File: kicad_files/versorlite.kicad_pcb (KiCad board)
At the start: 4 copper layers, 33 x 81.3 mm, 138 parts, among them J1 Conn_01x01_Socket, J10 IGN_2, J3 RFD900ux 10 Pin Header, J4 Conn_ARM_JTAG_SWD_10, J5 RFD900ux 3 Pin Power Select, J6 USB_C_Receptacle_USB2.0_16P, J7 Micro_SD_Card_Det2, J8 Conn_01x02_Socket, J9 IGN_1, Q1 FDMC510P-MS, Q2 AO3400A, Q3 AO3400A, SW1 SW_Push, SW2 SW_Push, U1 STM32F407VGTx, U10 W25Q128JVS, U11 LT1963AxST-3.3, U12 AP63205WU, U13 74LVC1G125, U2 MS5611-01BA, U3 BMI088, U4 MMC5983MA, U5 MAX-M10S, U6 BMP388, U7 LSM6DSM, U9 WE-TVS-82400102, Y1 LFXTAL036869Reel 8MHz Crystal

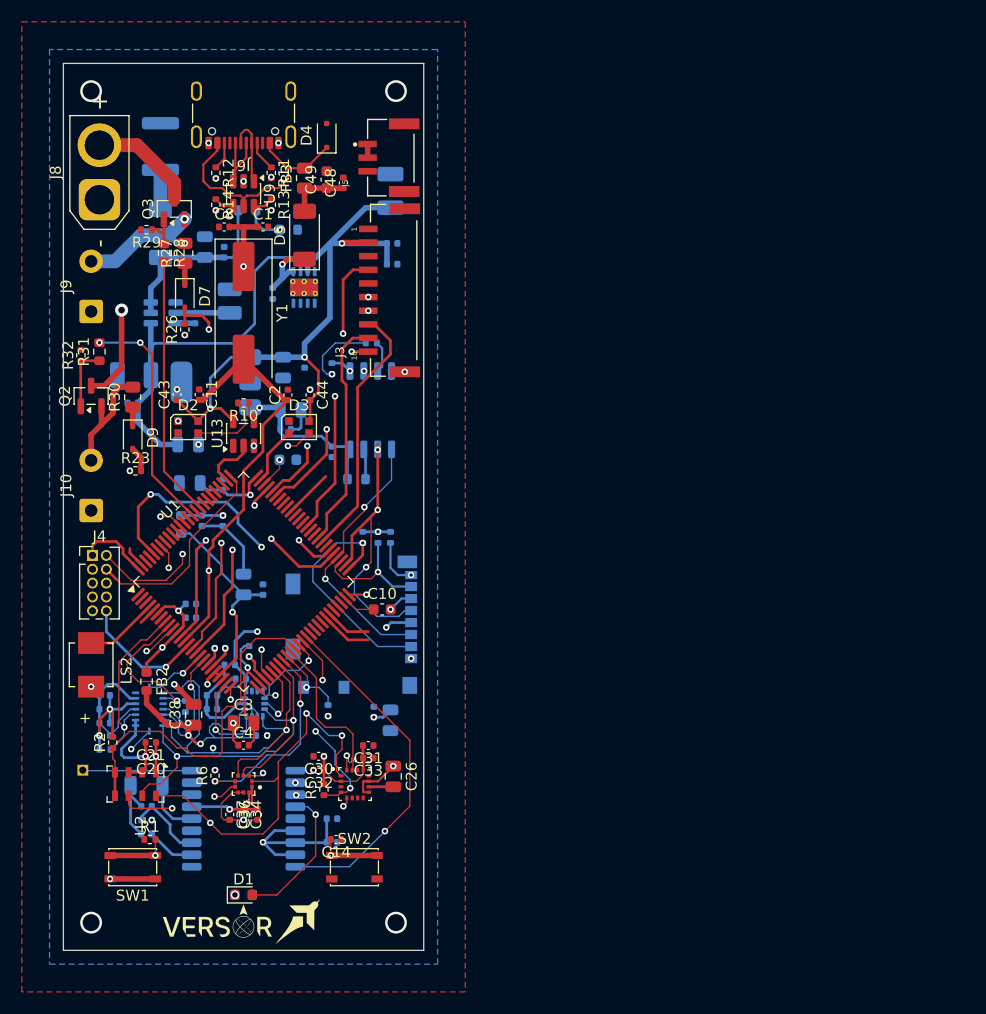
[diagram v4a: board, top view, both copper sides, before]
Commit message: fix mosfet, power traces, remove capacitors
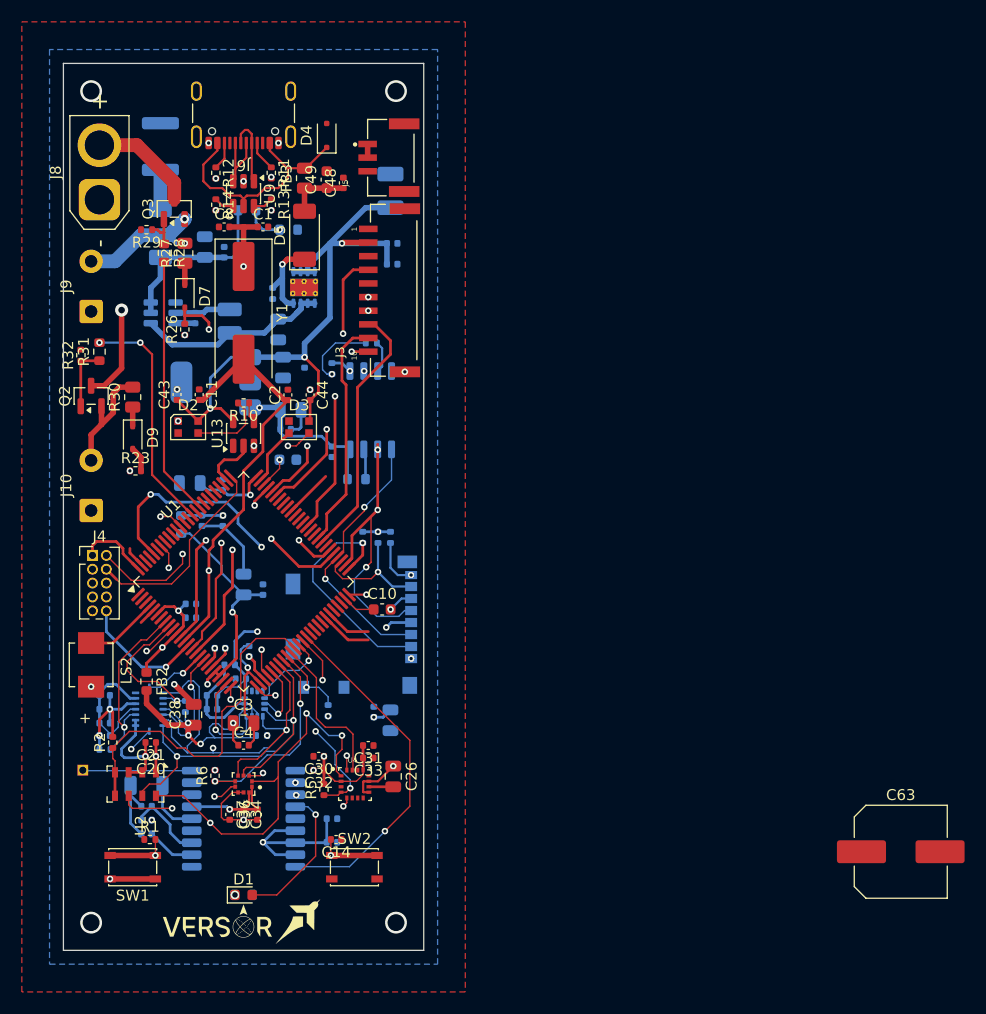
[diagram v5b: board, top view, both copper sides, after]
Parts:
- removed C57: 100μf, Capacitor_Tantalum_SMD:CP_EIA-3528-21_Kemet-B
- removed C59: 100nf, Capacitor_SMD:C_0402_1005Metric
- added C63: 470uF, Capacitor_SMD:C_Elec_8x10.2, F.Cu at (203.7, 134.5)
- moved C58 13.4 mm to (146.7, 86.6), turned to 90 degrees
- moved L1 1.84 mm to (142.2, 85.9), turned to 90 degrees
- turned Q1 to 90 degrees
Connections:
- Q1 pad 1: /Power/+VBUS -> Net-(Q1-S)
- Q1 pad 3: +5V -> Net-(Q1-S)
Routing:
- net Net-(Q1-S): track 37.9 -> 18.5 mm
- net +5V: track 57.2 -> 59.2 mm
- net /Power/+VBUS: track 6.09 -> 7.88 mm
- net GND: vias 22 -> 21

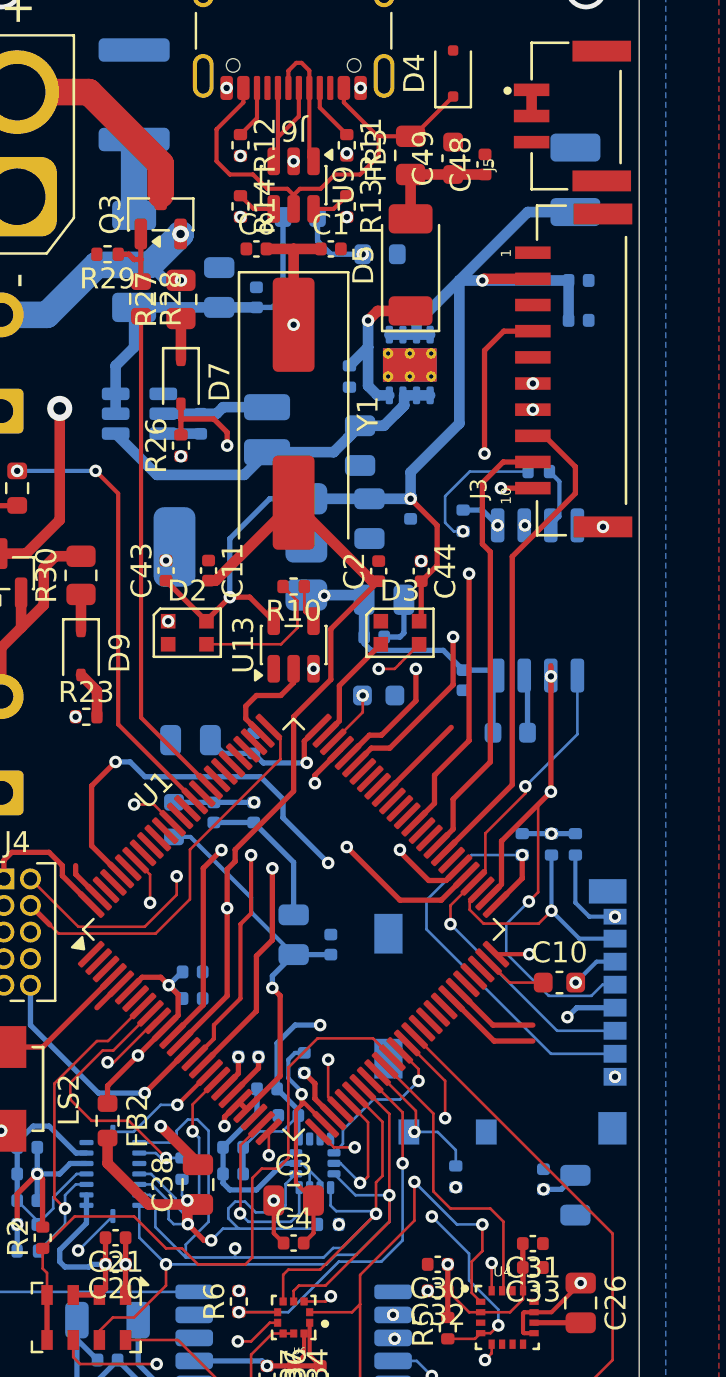
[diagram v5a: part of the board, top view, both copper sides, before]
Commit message: fix mcu decaps
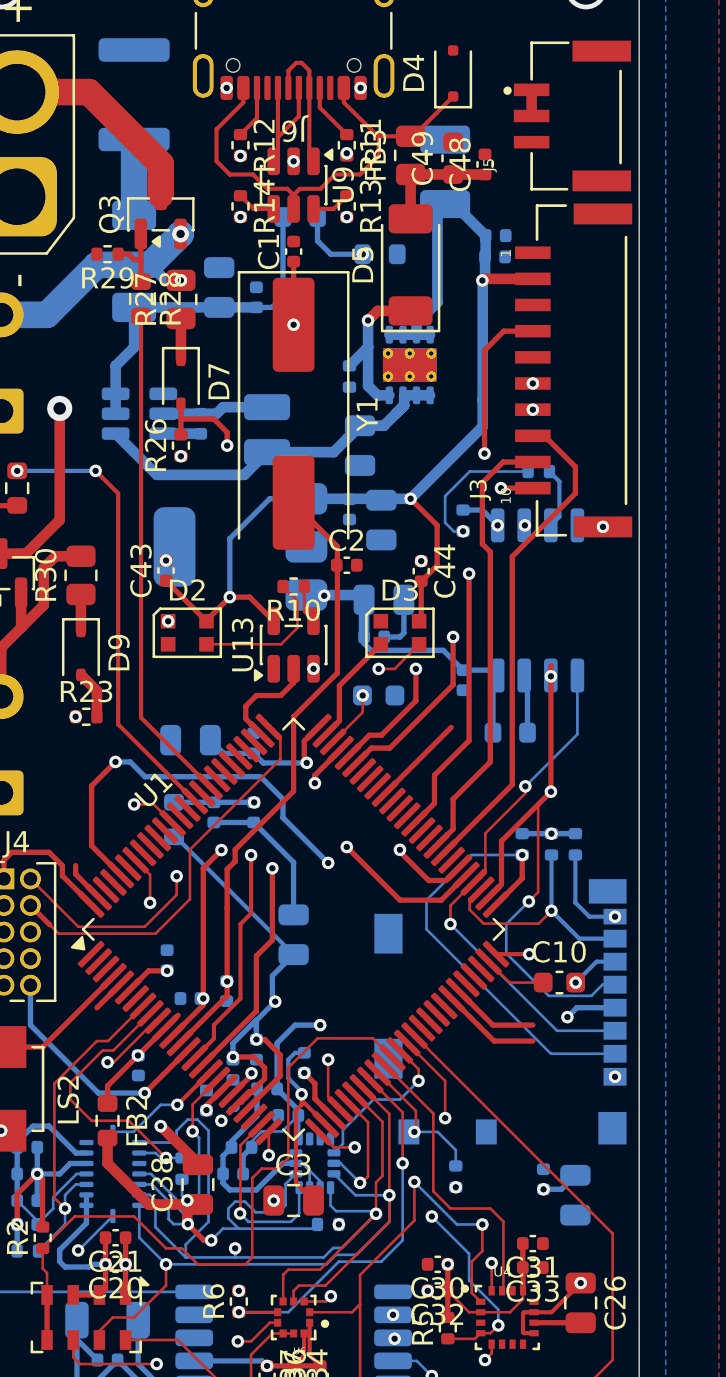
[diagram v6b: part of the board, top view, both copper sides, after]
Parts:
- C11, C4, C8: moved to B.Cu
- moved C8 36.0 mm to (138.6, 113.0)
- moved C11 20.1 mm to (140.3, 112.7), turned to 90 degrees
- moved C4 8.77 mm to (140.6, 116.4), turned to -90 degrees
- moved C47 6.23 mm to (150.7, 73.5)
- moved C19 6.15 mm to (141.7, 115.5), turned to -90 degrees
- moved C45 5.01 mm to (153.1, 77.6)
- moved C46 4.51 mm to (153.2, 76.6)
- moved C13 4.12 mm to (136.1, 116.2), turned to -90 degrees
- moved C55 2.92 mm to (146.2, 89.7)
- moved C9 2.89 mm to (139.3, 117.9), turned to 90 degrees
- moved C1 1.78 mm to (143.5, 77.3), turned to 90 degrees
- moved C2 1.55 mm to (146.1, 92.3), turned to 0 degrees
- moved C5 1.34 mm to (137.5, 111.2), turned to 90 degrees
- moved C56 0.57 mm to (147.7, 90.2)
- moved C42 0.40 mm to (141.0, 120.1)
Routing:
- net +3.3V_MAIN: track 111.6 -> 102.9 mm
- net /MCU/OSC_OUT: track 37.2 -> 29.8 mm
- net +5V: track 59.2 -> 53.8 mm
- net GND: track 99.9 -> 96.8 mm
- net /MCU/OSC_IN: track 52.9 -> 49.8 mm, vias 2 -> 3
- net +3V3_MCU: track 65.0 -> 67.1 mm, vias 4 -> 6
- net /MCU/EXTI0_BARO_LOW: track 38.3 -> 38.9 mm

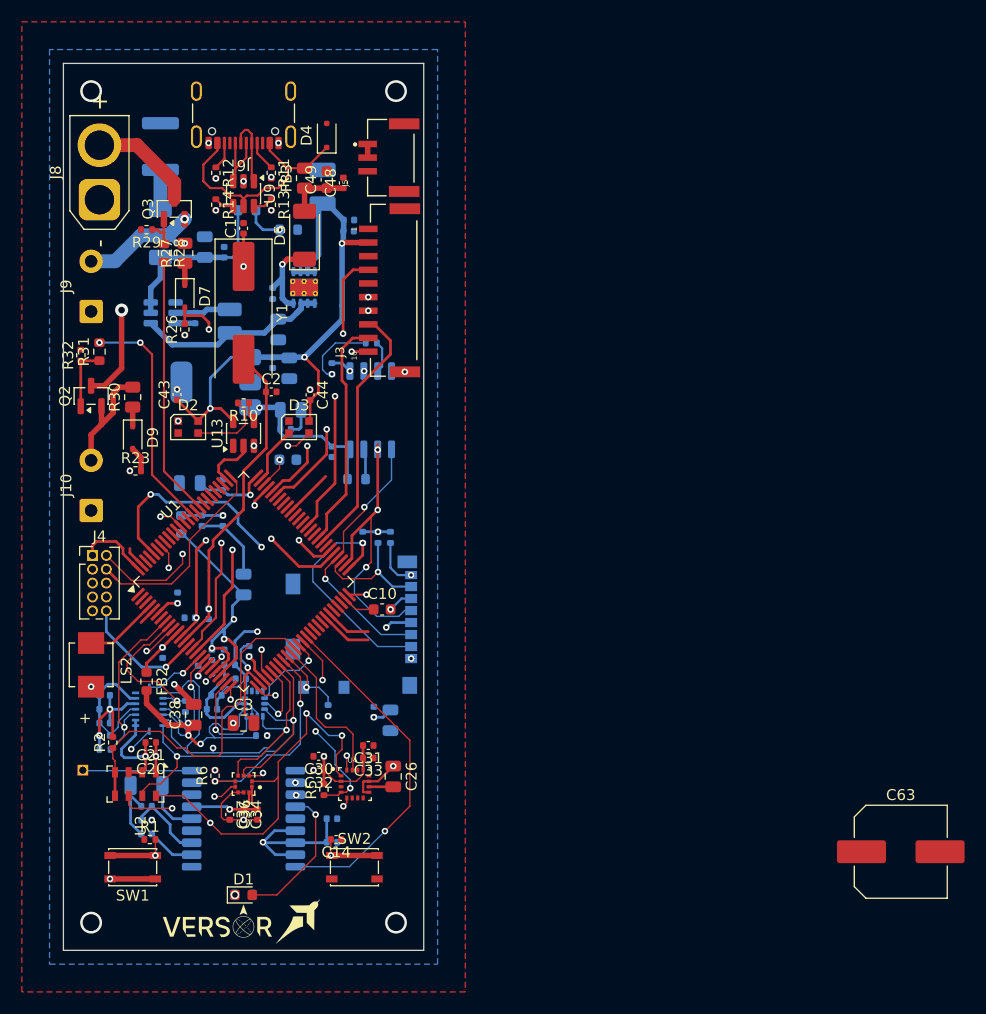
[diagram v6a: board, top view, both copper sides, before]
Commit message: Address all non-footprint DRC errors
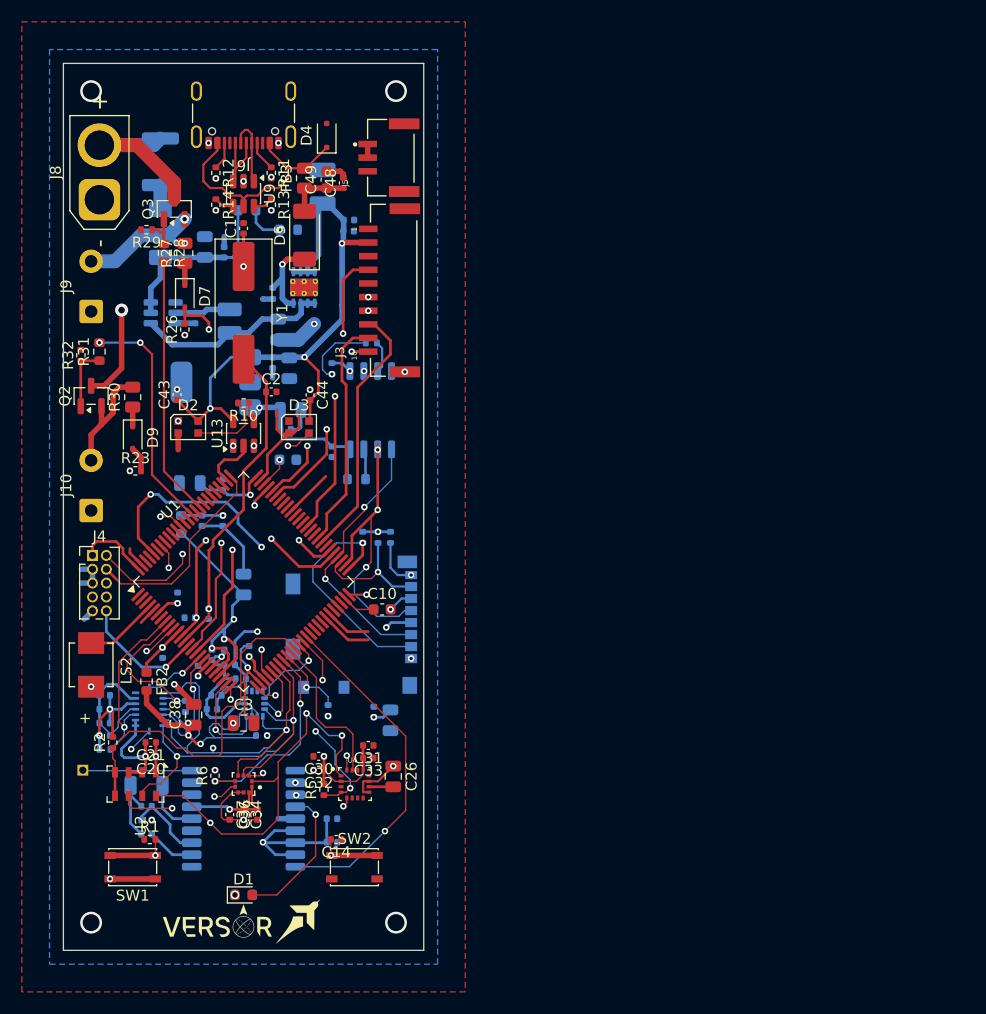
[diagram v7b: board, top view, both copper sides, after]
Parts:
- removed C63: 470uF, Capacitor_SMD:C_Elec_8x10.2
- moved F1 1.40 mm to (135.9, 71.2)
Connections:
- F1 pad 1: Net-(SW3-A) -> +9V
- Q1 pad 1: Net-(Q1-S) -> /Power/+VBUS
- Q1 pad 3: Net-(Q1-S) -> +5V
- SW1 pad 1: /MCU/3V3_MCU -> +3V3_MCU
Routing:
- net GND: track 96.8 -> 122.6 mm, vias 21 -> 23
- net +9V: track 36.2 -> 43.0 mm
- net +3V3_MCU: track 67.1 -> 73.1 mm, vias 6 -> 5
- net +3.3V_MAIN: track 102.9 -> 108.0 mm
- net Net-(D8-A): track 3.62 -> 2.23 mm
- net Net-(Q1-S): track 18.5 -> 17.9 mm

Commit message: Rearrange
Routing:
- net /MCU/SPI1_MISO: track 63.6 -> 62.3 mm
